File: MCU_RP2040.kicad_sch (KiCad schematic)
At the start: 34 parts, among them Q1 2N7002PV,115, X1 ECS-2520MVLC-120-CN

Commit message: Add dru, start routing
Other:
- moved on the sheet: C7
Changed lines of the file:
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@@
 	)
 	(junction
-		(at 55.88 72.39)
+		(at 48.26 72.39)
 		(diameter 0)
 		(color 0 0 0 0)
@@
 	(wire
 		(pts
-			(xy 55.88 80.01) (xy 55.88 78.74)
+			(xy 48.26 80.01) (xy 48.26 78.74)
 		)
 		(stroke
@@
 	(wire
 		(pts
-			(xy 49.53 72.39) (xy 55.88 72.39)
+			(xy 41.91 72.39) (xy 48.26 72.39)
 		)
 		(stroke
@@
 	(wire
 		(pts
-			(xy 55.88 73.66) (xy 55.88 72.39)
+			(xy 48.26 73.66) (xy 48.26 72.39)
 		)
 		(stroke
@@
 	(wire
 		(pts
-			(xy 55.88 72.39) (xy 59.69 72.39)
+			(xy 48.26 72.39) (xy 59.69 72.39)
 		)
 		(stroke
@@
 	(wire
 		(pts
-			(xy 49.53 80.01) (xy 55.88 80.01)
+			(xy 41.91 80.01) (xy 48.26 80.01)
 		)
 		(stroke
@@
 	)
 	(label "GND"
-		(at 49.53 80.01 0)
+		(at 41.91 80.01 0)
 		(fields_autoplaced yes)
 		(effects
@@
 	)
 	(label "3V3"
-		(at 49.53 72.39 0)
+		(at 41.91 72.39 0)
 		(fields_autoplaced yes)
 		(effects
@@
 	(symbol
 		(lib_id "Device:C_Small")
-		(at 55.88 76.2 0)
+		(at 48.26 76.2 0)
 		(unit 1)
 		(exclude_from_sim no)
@@
 		(fields_autoplaced yes)
 		(property "Reference" "C7"
-			(at 58.42 74.9362 0)
+			(at 50.8 74.9362 0)
 			(effects
 				(font
@@
 		)
 		(property "Value" "100nF"
-			(at 58.42 77.4762 0)
+			(at 50.8 77.4762 0)
 			(effects
 				(font
@@
 		)
 		(property "Footprint" "Capacitor_SMD:C_0402_1005Metric"
-			(at 55.88 76.2 0)
+			(at 48.26 76.2 0)
 			(effects
 				(font
@@
 		)
 		(property "Datasheet" "https://www.yageo.com/upload/media/product/productsearch/datasheet/mlcc/UPY-GPHC_X7R_6.3V-to-250V_24.pdf"
-			(at 55.88 76.2 0)
+			(at 48.26 76.2 0)
 			(effects
 				(font
@@
 		)
 		(property "Description" "0.1 µF ±10% 25V Ceramic Capacitor X7R 0402 (1005 Metric)"
-			(at 55.88 76.2 0)
+			(at 48.26 76.2 0)
 			(effects
 				(font
@@
 		)
 		(property "Price" "$0.17"
-			(at 55.88 76.2 0)
+			(at 48.26 76.2 0)
 			(effects
 				(font
@@
 		)
 		(property "Interface" ""
-			(at 55.88 76.2 0)
+			(at 48.26 76.2 0)
 			(effects
 				(font
@@
 		)
 		(property "Rating" "CAP 0402 50V 100 NF X7R"
-			(at 55.88 76.2 0)
+			(at 48.26 76.2 0)
 			(effects
 				(font
@@
 		)
 		(property "Supplier" "Digikey"
-			(at 55.88 76.2 0)
+			(at 48.26 76.2 0)
 			(effects
 				(font
@@
 		)
 		(property "Supplier PN" "13-CC0402KPX7R9BB104CT-ND"
-			(at 55.88 76.2 0)
+			(at 48.26 76.2 0)
 			(effects
 				(font
@@
 		)
 		(property "Manufacturer" "YAGEO"
-			(at 55.88 76.2 0)
+			(at 48.26 76.2 0)
 			(effects
 				(font
@@
 		)
 		(property "MPN" "CC0402KPX7R9BB104"
-			(at 55.88 76.2 0)
+			(at 48.26 76.2 0)
 			(effects
 				(font
@@
 		)
 		(property "Substitute" ""
-			(at 55.88 76.2 0)
+			(at 48.26 76.2 0)
 			(effects
 				(font
@@
 		)
 		(property "LCSC" "C432917"
-			(at 55.88 76.2 0)
+			(at 48.26 76.2 0)
 			(effects
 				(font

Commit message: Finish off routing
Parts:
- removed TP?: Boot, TestPoint:TestPoint_Pad_D1.0mm, symbol Connector:TestPoint
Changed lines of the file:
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@@
 	)
 	(junction
-		(at 109.22 166.37)
-		(diameter 0)
-		(color 0 0 0 0)
-	)
-	(junction
 		(at 153.67 27.94)
 		(diameter 0)
@@
 	(wire
 		(pts
-			(xy 110.49 166.37) (xy 109.22 166.37)
-		)
-		(stroke
-			(width 0)
-			(type default)
-		)
-	)
-	(wire
-		(pts
 			(xy 224.79 38.1) (xy 224.79 43.18)
 		)
@@
 	(wire
 		(pts
-			(xy 109.22 166.37) (xy 109.22 167.64)
+			(xy 109.22 165.1) (xy 109.22 167.64)
 		)
 		(stroke
@@
 	(wire
 		(pts
-			(xy 109.22 165.1) (xy 109.22 166.37)
-		)
-		(stroke
-			(width 0)
-			(type default)
-		)
-	)
-	(wire
-		(pts
 			(xy 142.24 43.18) (xy 153.67 43.18)
 		)
@@
 					(unit 1)
 				)
-			)
-		)
-	)
-	(symbol
-		(lib_id "Connector:TestPoint")
-		(at 110.49 166.37 270)
-		(unit 1)
-		(exclude_from_sim no)
-		(in_bom no)
-		(on_board yes)
-		(dnp no)
-		(fields_autoplaced yes)
-		(property "Reference" "TP?"
-			(at 115.57 165.0999 90)
-			(effects
-				(font
-					(size 1.27 1.27)
-				)
-				(justify left)
-			)
-		)
-		(property "Value" "Boot"
-			(at 115.57 167.6399 90)
-			(effects
-				(font
-					(size 1.27 1.27)
-				)
-				(justify left)
-			)
-		)
-		(property "Footprint" "TestPoint:TestPoint_Pad_D1.0mm"
-			(at 110.49 171.45 0)
-			(effects
-				(font
-					(size 1.27 1.27)
-				)
-				(hide yes)
-			)
-		)
-		(property "Datasheet" ""
-			(at 110.49 171.45 0)
-			(effects
-				(font
-					(size 1.27 1.27)
-				)
-				(hide yes)
-			)
-		)
-		(property "Description" ""
-			(at 110.49 166.37 0)
-			(effects
-				(font
-					(size 1.27 1.27)
-				)
-				(hide yes)
-			)
-		)
-		(property "Substitute" ""
-			(at 110.49 166.37 0)
-			(effects
-				(font
-					(size 1.27 1.27)
-				)
-				(hide yes)
-			)
-		)
-		(property "LCSC" ""
-			(at 110.49 166.37 0)
-			(effects
-				(font
-					(size 1.27 1.27)
-				)
-				(hide yes)
-			)
-		)
-		(pin "1"
-		)
-		(instances
-			(project "RP2040"
-				(path "/ba62e47e-9e07-4e97-ab08-24b670d50f97/f42afd4d-da97-4905-9d8b-11c28a037c21"
-					(reference "TP?")
-					(unit 1)
-				)
-			)
-			(project "Mad_RP2040"
-				(path "/eedae293-eb5b-47bd-b383-bccfdf81bf72/4e3cb99d-3a42-46ca-abb7-444fcb451820/f42afd4d-da97-4905-9d8b-11c28a037c21"
-					(reference "TP3")
-					(unit 1)
-				)

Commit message: Minor silk update
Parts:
- TP?: value Delay -> DELAY
- TP?: value Reset -> RESET
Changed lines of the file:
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@@
 			)
 		)
-		(property "Value" "Delay"
+		(property "Value" "DELAY"
 			(at 96.52 169.4179 0)
 			(effects
@@
 			)
 		)
-		(property "Value" "Reset"
+		(property "Value" "RESET"
 			(at 73.66 168.9099 90)
 			(effects

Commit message: 1 Add Panel (#2)
* #1 Add panel file and updated github action

* #1 Test for if panel file exhists

* #1 Rejig github actions

* Update job descriptions

* Add board tabs

* adjust panel array

* Add verbose

* Try using container method for building datapack

* Test custom action

* Update workflow

* Minor track work update and

* Add USB diff trace calcs and reroute usb traces

* Enable verbose

* Comment out second build

* Update value to mpn

* Update value to mpn

* #2 Update panel tabs
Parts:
- added TP5: XTAL_OUT, TestPoint:TestPoint_Pad_D1.0mm, symbol Connector:TestPoint
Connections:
- net at U?.21 (XTAL_OUT): now also TP5.1
- no-connect marks 1 -> 0
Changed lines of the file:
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@@
 		(color 0 0 0 0)
 	)
-	(no_connect
-		(at 177.8 96.52)
-	)
 	(wire
 		(pts
@@
 					(unit 1)
 				)
+			)
+		)
+	)
+	(symbol
+		(lib_id "Connector:TestPoint")
+		(at 177.8 96.52 90)
+		(mirror x)
+		(unit 1)
+		(exclude_from_sim no)
+		(in_bom no)
+		(on_board yes)
+		(dnp no)
+		(property "Reference" "TP5"
+			(at 172.72 95.2499 90)
+			(effects
+				(font
+					(size 1.27 1.27)
+				)
+				(justify left)
+			)
+		)
+		(property "Value" "XTAL_OUT"
+			(at 172.72 97.7899 90)
+			(effects
+				(font
+					(size 1.27 1.27)
+				)
+				(justify left)
+			)
+		)
+		(property "Footprint" "TestPoint:TestPoint_Pad_D1.0mm"
+			(at 177.8 101.6 0)
+			(effects
+				(font
+					(size 1.27 1.27)
+				)
+				(hide yes)
+			)
+		)
+		(property "Datasheet" ""
+			(at 177.8 101.6 0)
+			(effects
+				(font
+					(size 1.27 1.27)
+				)
+				(hide yes)
+			)
+		)
+		(property "Description" ""
+			(at 177.8 96.52 0)
+			(effects
+				(font
+					(size 1.27 1.27)
+				)
+				(hide yes)
+			)
+		)
+		(property "Price" ""
+			(at 177.8 96.52 0)
+			(effects
+				(font
+					(size 1.27 1.27)
+				)
+				(hide yes)
+			)
+		)
+		(property "Interface" ""
+			(at 177.8 96.52 0)
+			(effects
+				(font
+					(size 1.27 1.27)
+				)
+				(hide yes)
+			)
+		)
+		(property "Rating" ""
+			(at 177.8 96.52 0)
+			(effects
+				(font
+					(size 1.27 1.27)
+				)
+				(hide yes)
+			)
+		)
+		(property "Supplier" ""
+			(at 177.8 96.52 0)
+			(effects
+				(font
+					(size 1.27 1.27)
+				)
+				(hide yes)
+			)
+		)
+		(property "Supplier PN" ""
+			(at 177.8 96.52 0)
+			(effects
+				(font
+					(size 1.27 1.27)
+				)
+				(hide yes)
+			)
+		)
+		(property "Manufacturer" ""
+			(at 177.8 96.52 0)
+			(effects
+				(font
+					(size 1.27 1.27)
+				)
+				(hide yes)
+			)
+		)
+		(property "MPN" ""
+			(at 177.8 96.52 0)
+			(effects
+				(font
+					(size 1.27 1.27)
+				)
+				(hide yes)
+			)
+		)
+		(property "Substitute" ""
+			(at 177.8 96.52 0)
+			(effects
+				(font
+					(size 1.27 1.27)
+				)
+				(hide yes)
+			)
+		)
+		(property "LCSC" ""
+			(at 177.8 96.52 0)
+			(effects
+				(font
+					(size 1.27 1.27)
+				)
+				(hide yes)
+			)
+		)
+		(pin "1"
+		)
+		(instances
+			(project "Mad_RP2040"
+				(path "/eedae293-eb5b-47bd-b383-bccfdf81bf72/4e3cb99d-3a42-46ca-abb7-444fcb451820/f42afd4d-da97-4905-9d8b-11c28a037c21"
+					(reference "TP5")
+					(unit 1)
+				)

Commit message: Update usb data pins, update to fix 3v3 reg not adj
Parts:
- removed TP5: XTAL_OUT, TestPoint:TestPoint_Pad_D1.0mm, symbol Connector:TestPoint
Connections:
- no-connect marks 0 -> 1
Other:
- note removed: "C113767"
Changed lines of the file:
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@@
 		(color 0 0 0 0)
 	)
+	(no_connect
+		(at 184.15 96.52)
+	)
 	(wire
 		(pts
@@
 	(wire
 		(pts
-			(xy 177.8 96.52) (xy 184.15 96.52)
-		)
-		(stroke
-			(width 0)
-			(type default)
-		)
-	)
-	(wire
-		(pts
 			(xy 54.61 110.49) (xy 54.61 114.3)
 		)
@@
 	(text "Q1B - pulls ~{CS} to GND"
 		(exclude_from_sim no)
-		(at 106.68 182.88 0)
+		(at 111.76 179.07 0)
 		(effects
 			(font
@@
 		)
 	)
-	(text "C113767"
-		(exclude_from_sim no)
-		(at 83.82 104.14 0)
-		(effects
-			(font
-				(size 1.27 1.27)
-			)
-		)
-	)
 	(text "Removed inverter as\nwe don't care about \nbeing backwards \ncompatable."
 		(exclude_from_sim no)
@@
 		)
 	)
-	(label "GND"
-		(at 171.45 160.02 0)
-		(fields_autoplaced yes)
-		(effects
-			(font
-				(size 1.27 1.27)
-			)
-			(justify left bottom)
-		)
-	)
 	(label "3V3"
 		(at 41.91 72.39 0)
@@
 		)
 	)
+	(hierarchical_label "GND"
+		(shape input)
+		(at 171.45 160.02 180)
+		(fields_autoplaced yes)
+		(effects
+			(font
+				(size 1.27 1.27)
+			)
+			(justify right)
+		)
+	)
 	(hierarchical_label "GPIO2"
 		(shape bidirectional)
@@
 					(unit 1)
 				)
-			)
-		)
-	)
-	(symbol
-		(lib_id "Connector:TestPoint")
-		(at 177.8 96.52 90)
-		(mirror x)
-		(unit 1)
-		(exclude_from_sim no)
-		(in_bom no)
-		(on_board yes)
-		(dnp no)
-		(property "Reference" "TP5"
-			(at 172.72 95.2499 90)
-			(effects
-				(font
-					(size 1.27 1.27)
-				)
-				(justify left)
-			)
-		)
-		(property "Value" "XTAL_OUT"
-			(at 172.72 97.7899 90)
-			(effects
-				(font
-					(size 1.27 1.27)
-				)
-				(justify left)
-			)
-		)
-		(property "Footprint" "TestPoint:TestPoint_Pad_D1.0mm"
-			(at 177.8 101.6 0)
-			(effects
-				(font
-					(size 1.27 1.27)
-				)
-				(hide yes)
-			)
-		)
-		(property "Datasheet" ""
-			(at 177.8 101.6 0)
-			(effects
-				(font
-					(size 1.27 1.27)
-				)
-				(hide yes)
-			)
-		)
-		(property "Description" ""
-			(at 177.8 96.52 0)
-			(effects
-				(font
-					(size 1.27 1.27)
-				)
-				(hide yes)
-			)
-		)
-		(property "Price" ""
-			(at 177.8 96.52 0)
-			(effects
-				(font
-					(size 1.27 1.27)
-				)
-				(hide yes)
-			)
-		)
-		(property "Interface" ""
-			(at 177.8 96.52 0)
-			(effects
-				(font
-					(size 1.27 1.27)
-				)
-				(hide yes)
-			)
-		)
-		(property "Rating" ""
-			(at 177.8 96.52 0)
-			(effects
-				(font
-					(size 1.27 1.27)
-				)
-				(hide yes)
-			)
-		)
-		(property "Supplier" ""
-			(at 177.8 96.52 0)
-			(effects
-				(font
-					(size 1.27 1.27)
-				)
-				(hide yes)
-			)
-		)
-		(property "Supplier PN" ""
-			(at 177.8 96.52 0)
-			(effects
-				(font
-					(size 1.27 1.27)
-				)
-				(hide yes)
-			)
-		)
-		(property "Manufacturer" ""
-			(at 177.8 96.52 0)
-			(effects
-				(font
-					(size 1.27 1.27)
-				)
-				(hide yes)
-			)
-		)
-		(property "MPN" ""
-			(at 177.8 96.52 0)
-			(effects
-				(font
-					(size 1.27 1.27)
-				)
-				(hide yes)
-			)
-		)
-		(property "Substitute" ""
-			(at 177.8 96.52 0)
-			(effects
-				(font
-					(size 1.27 1.27)
-				)
-				(hide yes)
-			)
-		)
-		(property "LCSC" ""
-			(at 177.8 96.52 0)
-			(effects
-				(font
-					(size 1.27 1.27)
-				)
-				(hide yes)
-			)
-		)
-		(pin "1"
-		)
-		(instances
-			(project "Mad_RP2040"
-				(path "/eedae293-eb5b-47bd-b383-bccfdf81bf72/4e3cb99d-3a42-46ca-abb7-444fcb451820/f42afd4d-da97-4905-9d8b-11c28a037c21"
-					(reference "TP5")
-					(unit 1)
-				)

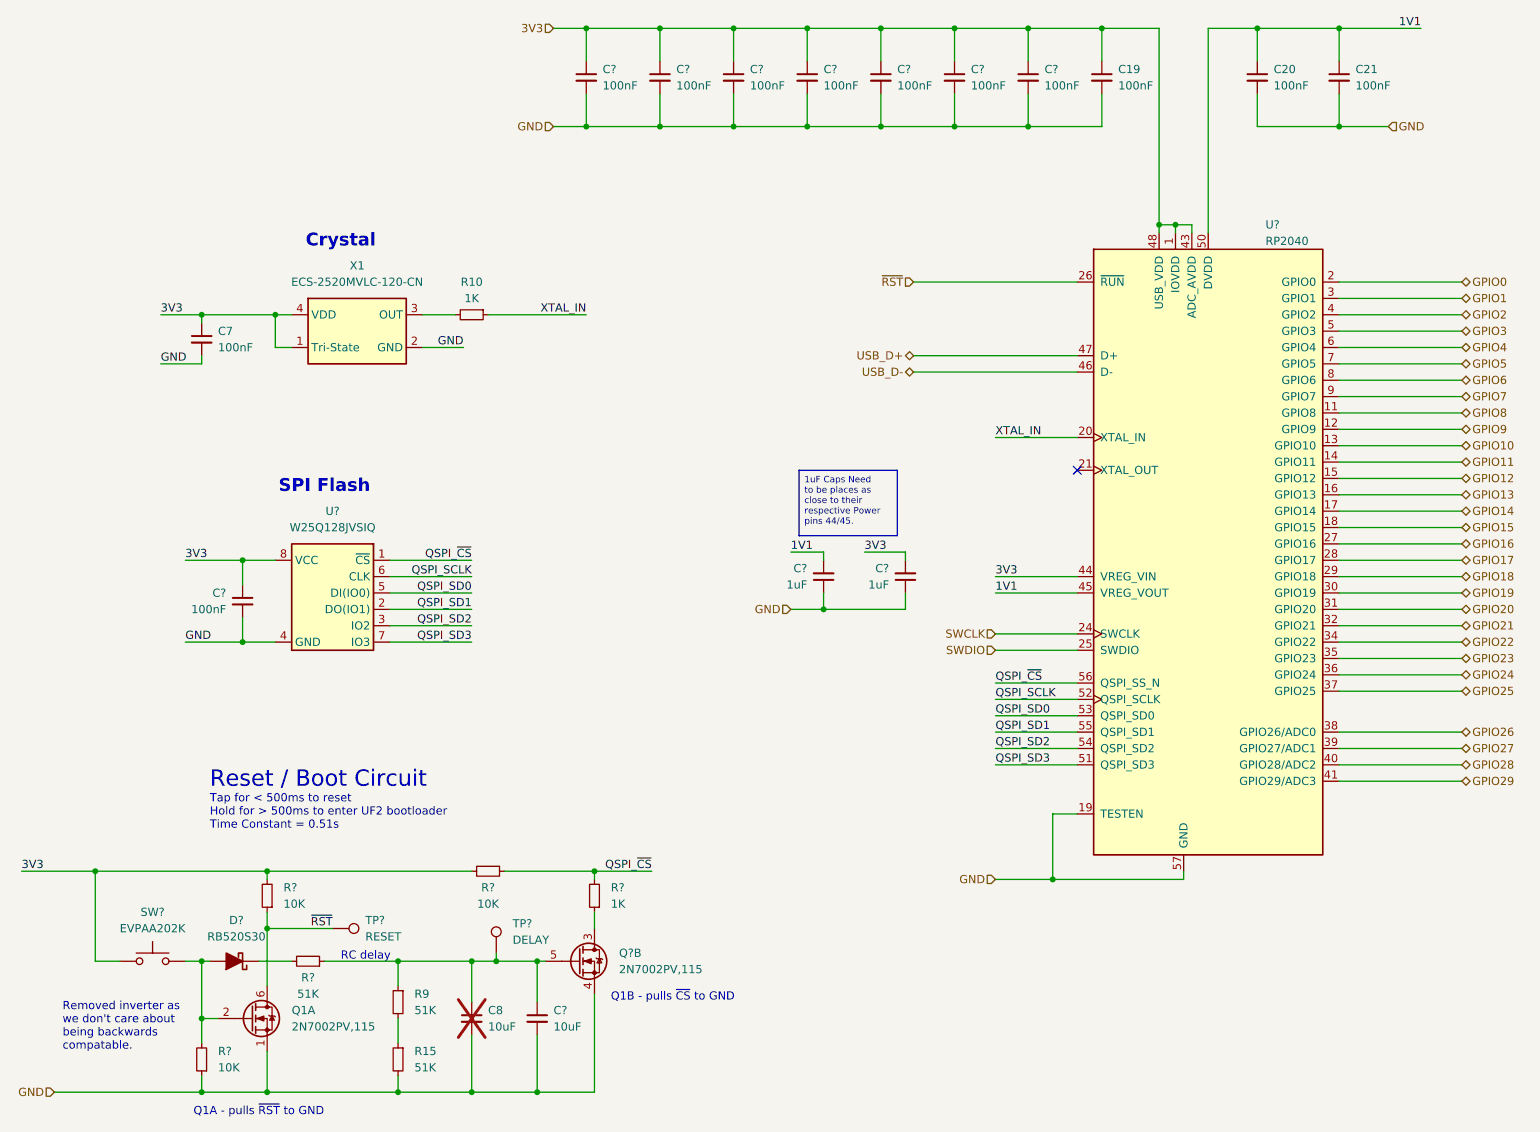
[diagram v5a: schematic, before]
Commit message: Update footprint on back light SK6812MINI LED, add more back lights.
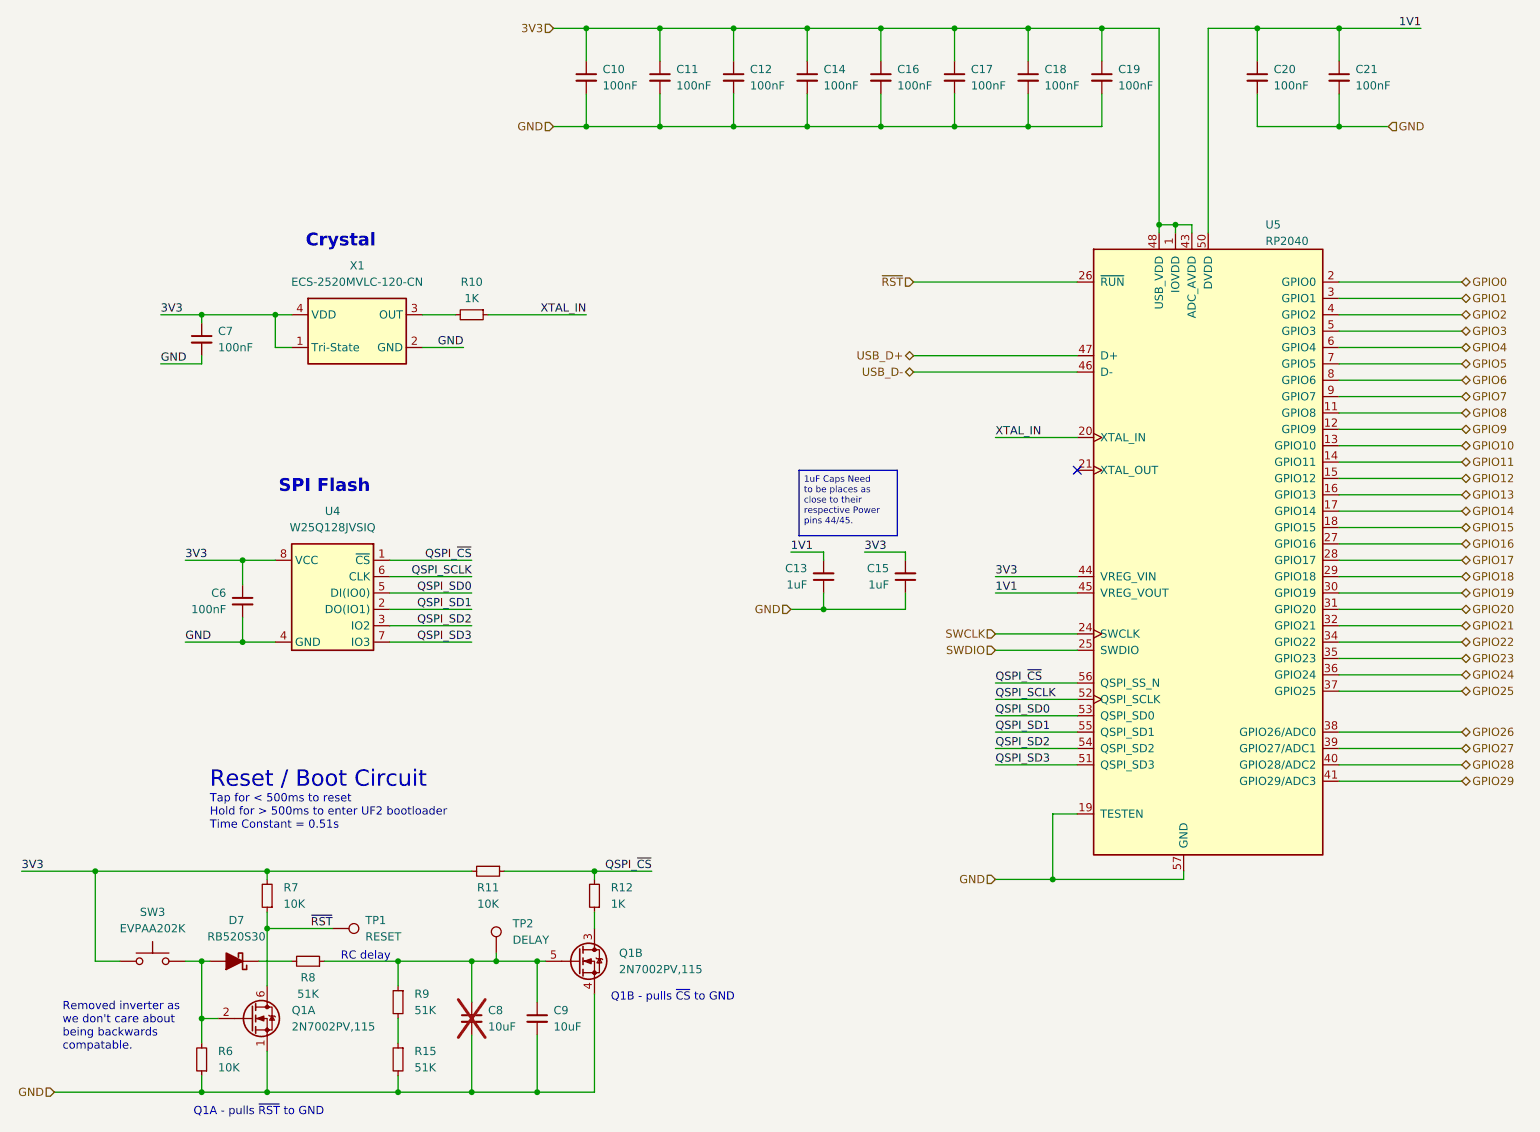
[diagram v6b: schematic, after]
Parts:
- gave numbers to parts that had none: 23

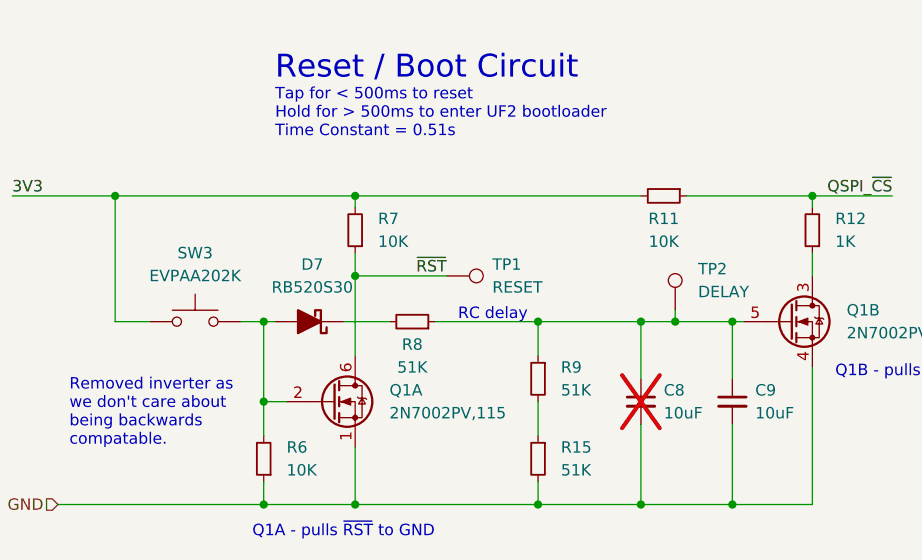
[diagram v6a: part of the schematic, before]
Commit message: Expand board to 4x5, update rev to b
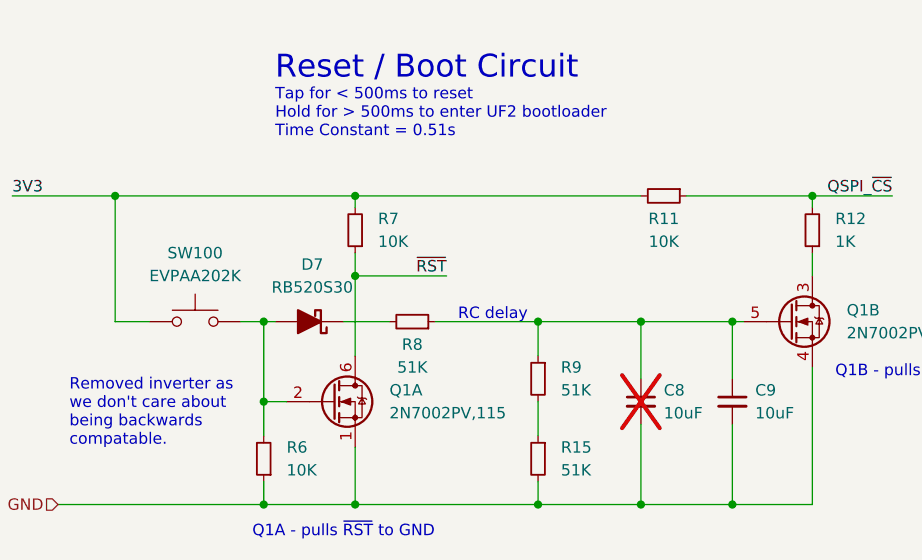
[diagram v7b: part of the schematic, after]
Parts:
- removed TP1: RESET, TestPoint:TestPoint_Pad_D1.0mm, symbol Connector:TestPoint
- removed TP2: DELAY, TestPoint:TestPoint_Pad_D1.0mm, symbol Connector:TestPoint
- renumbered SW3 to SW100
